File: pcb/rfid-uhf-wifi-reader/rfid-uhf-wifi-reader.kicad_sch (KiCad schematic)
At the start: 15 parts, among them P1 USB_C_Plug, Q1 BSS138, Q2 BSS138, SW1 SW_Push, SW2 SW_Push, U1 ESP32-WROOM-32, U2 AMS1117-3.3, U3 CH340E

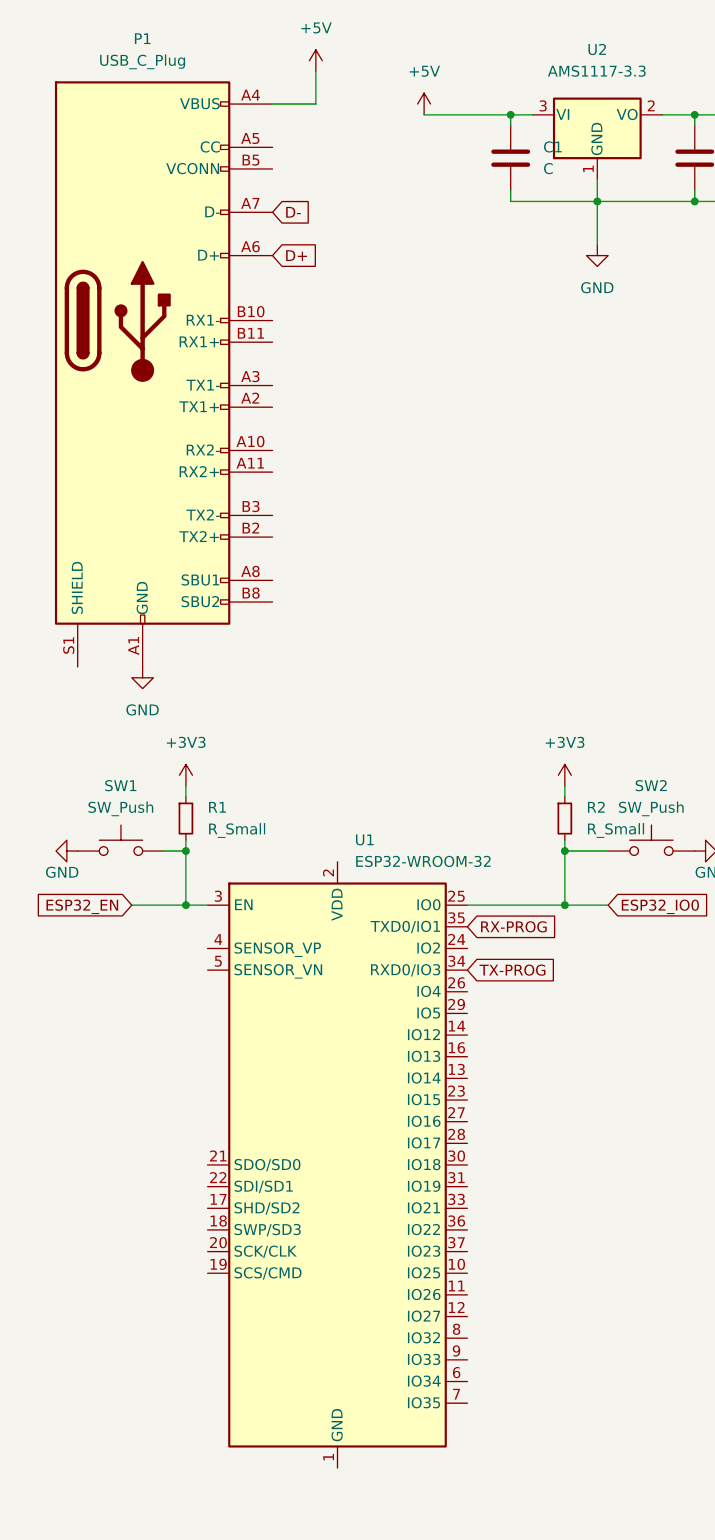
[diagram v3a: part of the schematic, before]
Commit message: update components
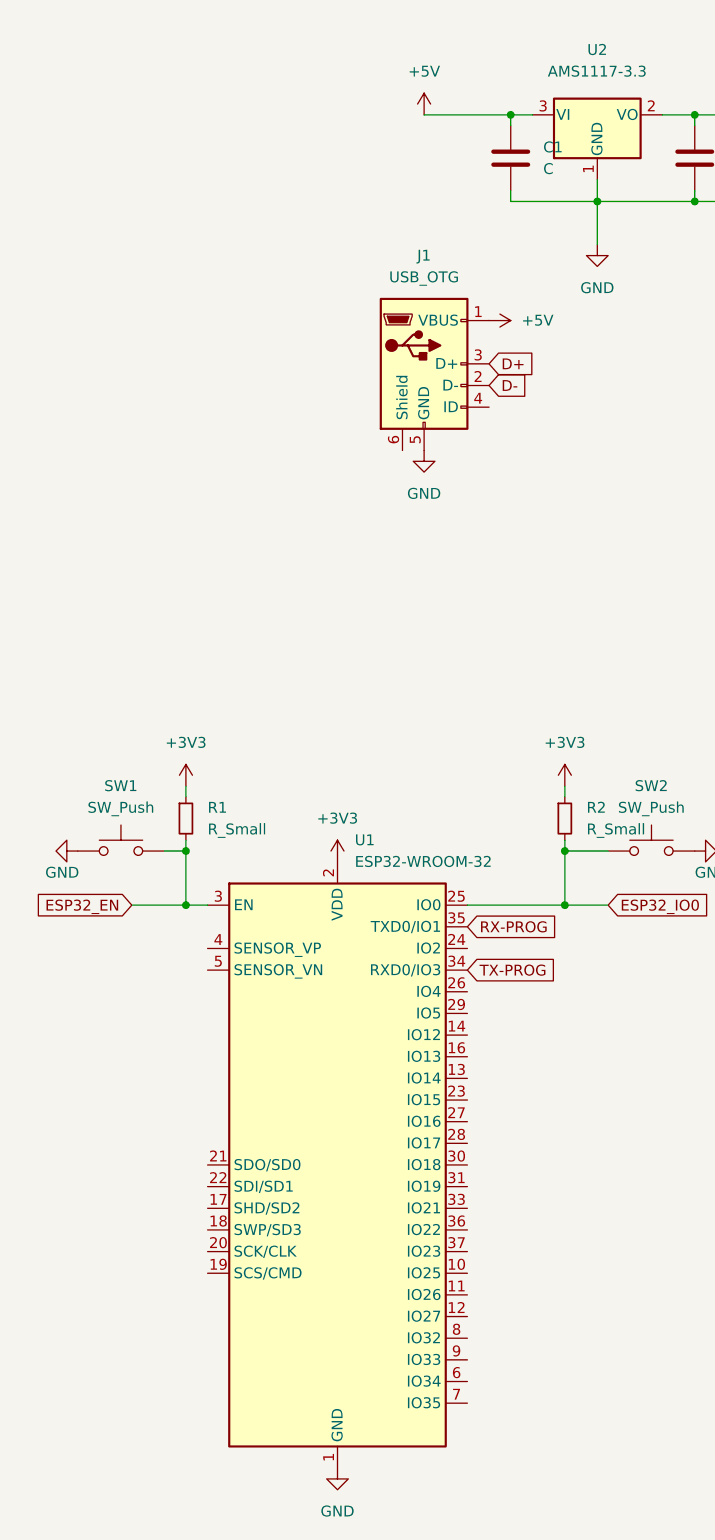
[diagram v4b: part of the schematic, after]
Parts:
- removed P1: USB_C_Plug, Connector_USB:USB_C_Plug_Molex_105444, symbol Connector:USB_C_Plug
- added J1: USB_OTG, Connector_USB:USB_Micro-B_Amphenol_10118194_Horizontal, symbol Connector:USB_OTG
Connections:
- net +3V3: now also U1.2 (VDD)
- net +5V: now also J1.1 (VBUS)
- net D+: now also J1.3 (D+)
- net D-: now also J1.2 (D-)
- net GND: now also U1.1 (GND), U1.15 (GND), U1.38 (GND), U1.39 (GND), J1.5 (GND)
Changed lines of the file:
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@@
-    (stroke (width 0) (type default) (color 0 0 0 0))
-  )
-  (wire (pts (xy 48.26 22.86) (xy 48.26 19.05))
     (stroke (width 0) (type default) (color 0 0 0 0))
   )
@@
   )
   (wire (pts (xy 101.6 33.02) (xy 101.6 34.29))
-    (stroke (width 0) (type default) (color 0 0 0 0))
-  )
-  (wire (pts (xy 43.18 22.86) (xy 48.26 22.86))
     (stroke (width 0) (type default) (color 0 0 0 0))
   )
@@
     )
   )
-  (global_label "D+" (shape input) (at 43.18 40.64 0) (fields_autoplaced)
+  (global_label "D+" (shape input) (at 68.58 53.34 0) (fields_autoplaced)
     (effects (font (size 1.27 1.27)) (justify left))
-    (property "Intersheet References" "${INTERSHEET_REFS}" (id 0) (at 48.4355 40.5606 0)
+    (property "Intersheet References" "${INTERSHEET_REFS}" (id 0) (at 73.8355 53.2606 0)
       (effects (font (size 1.27 1.27)) (justify left) hide)
     )
@@
     )
   )
-  (global_label "D-" (shape input) (at 43.18 35.56 0) (fields_autoplaced)
+  (global_label "D-" (shape input) (at 68.58 55.88 0) (fields_autoplaced)
     (effects (font (size 1.27 1.27)) (justify left))
-    (property "Intersheet References" "${INTERSHEET_REFS}" (id 0) (at 48.4355 35.4806 0)
+    (property "Intersheet References" "${INTERSHEET_REFS}" (id 0) (at 73.8355 55.8006 0)
       (effects (font (size 1.27 1.27)) (justify left) hide)
     )
@@
     )
     (property "Datasheet" "" (id 3) (at 194.31 52.07 0)
+      (effects (font (size 1.27 1.27)) hide)
+    )
+    (pin "1")
+  )
+  (symbol (lib_id "power:+3V3") (at 50.8 111.76 0) (unit 1)
+    (in_bom yes) (on_board yes) (fields_autoplaced)
+    (property "Reference" "#PWR0114" (id 0) (at 50.8 115.57 0)
+      (effects (font (size 1.27 1.27)) hide)
+    )
+    (property "Value" "+3V3" (id 1) (at 50.8 106.68 0))
+    (property "Footprint" "" (id 2) (at 50.8 111.76 0)
+      (effects (font (size 1.27 1.27)) hide)
+    )
+    (property "Datasheet" "" (id 3) (at 50.8 111.76 0)
       (effects (font (size 1.27 1.27)) hide)
     )
@@
     (pin "3")
   )
-  (symbol (lib_id "Connector:USB_C_Plug") (at 27.94 48.26 0) (unit 1)
-    (in_bom yes) (on_board yes) (fields_autoplaced)
-    (property "Reference" "P1" (id 0) (at 27.94 15.24 0))
-    (property "Value" "USB_C_Plug" (id 1) (at 27.94 17.78 0))
-    (property "Footprint" "Connector_USB:USB_C_Plug_Molex_105444" (id 2) (at 31.75 48.26 0)
-      (effects (font (size 1.27 1.27)) hide)
-    )
-    (property "Datasheet" "https://www.usb.org/sites/default/files/documents/usb_type-c.zip" (id 3) (at 31.75 48.26 0)
-      (effects (font (size 1.27 1.27)) hide)
-    )
-    (pin "A1")
-    (pin "A10")
-    (pin "A11")
-    (pin "A12")
-    (pin "A2")
-    (pin "A3")
-    (pin "A4")
-    (pin "A5")
-    (pin "A6")
-    (pin "A7")
-    (pin "A8")
-    (pin "A9")
-    (pin "B1")
-    (pin "B10")
-    (pin "B11")
-    (pin "B12")
-    (pin "B2")
-    (pin "B3")
-    (pin "B4")
-    (pin "B5")
-    (pin "B8")
-    (pin "B9")
-    (pin "S1")
+  (symbol (lib_id "power:GND") (at 50.8 182.88 0) (unit 1)
+    (in_bom yes) (on_board yes) (fields_autoplaced)
+    (property "Reference" "#PWR0115" (id 0) (at 50.8 189.23 0)
+      (effects (font (size 1.27 1.27)) hide)
+    )
+    (property "Value" "GND" (id 1) (at 50.8 187.96 0))
+    (property "Footprint" "" (id 2) (at 50.8 182.88 0)
+      (effects (font (size 1.27 1.27)) hide)
+    )
+    (property "Datasheet" "" (id 3) (at 50.8 182.88 0)
+      (effects (font (size 1.27 1.27)) hide)
+    )
+    (pin "1")
   )
   (symbol (lib_id "Device:C") (at 194.31 48.26 0) (unit 1)
@@
     (pin "9")
   )
+  (symbol (lib_id "Connector:USB_OTG") (at 60.96 53.34 0) (unit 1)
+    (in_bom yes) (on_board yes) (fields_autoplaced)
+    (property "Reference" "J1" (id 0) (at 60.96 40.64 0))
+    (property "Value" "USB_OTG" (id 1) (at 60.96 43.18 0))
+    (property "Footprint" "Connector_USB:USB_Micro-B_Amphenol_10118194_Horizontal" (id 2) (at 64.77 54.61 0)
+      (effects (font (size 1.27 1.27)) hide)
+    )
+    (property "Datasheet" " ~" (id 3) (at 64.77 54.61 0)
+      (effects (font (size 1.27 1.27)) hide)
+    )
+    (pin "1")
+    (pin "2")
+    (pin "3")
+    (pin "4")
+    (pin "5")
+    (pin "6")
+  )
   (symbol (lib_id "power:+3V3") (at 77.47 102.87 0) (unit 1)
     (in_bom yes) (on_board yes) (fields_autoplaced)
@@
     (pin "2")
   )
-  (symbol (lib_id "power:GND") (at 27.94 88.9 0) (unit 1)
-    (in_bom yes) (on_board yes) (fields_autoplaced)
-    (property "Reference" "#PWR0109" (id 0) (at 27.94 95.25 0)
-      (effects (font (size 1.27 1.27)) hide)
-    )
-    (property "Value" "GND" (id 1) (at 27.94 93.98 0))
-    (property "Footprint" "" (id 2) (at 27.94 88.9 0)
-      (effects (font (size 1.27 1.27)) hide)
-    )
-    (property "Datasheet" "" (id 3) (at 27.94 88.9 0)
+  (symbol (lib_id "power:GND") (at 60.96 63.5 0) (unit 1)
+    (in_bom yes) (on_board yes) (fields_autoplaced)
+    (property "Reference" "#PWR0109" (id 0) (at 60.96 69.85 0)
+      (effects (font (size 1.27 1.27)) hide)
+    )
+    (property "Value" "GND" (id 1) (at 60.96 68.58 0))
+    (property "Footprint" "" (id 2) (at 60.96 63.5 0)
+      (effects (font (size 1.27 1.27)) hide)
+    )
+    (property "Datasheet" "" (id 3) (at 60.96 63.5 0)
       (effects (font (size 1.27 1.27)) hide)
     )
@@
     (pin "1")
   )
-  (symbol (lib_id "power:+5V") (at 48.26 19.05 0) (unit 1)
-    (in_bom yes) (on_board yes) (fields_autoplaced)
-    (property "Reference" "#PWR0108" (id 0) (at 48.26 22.86 0)
-      (effects (font (size 1.27 1.27)) hide)
-    )
-    (property "Value" "+5V" (id 1) (at 48.26 13.97 0))
-    (property "Footprint" "" (id 2) (at 48.26 19.05 0)
-      (effects (font (size 1.27 1.27)) hide)
-    )
-    (property "Datasheet" "" (id 3) (at 48.26 19.05 0)
+  (symbol (lib_id "power:+5V") (at 68.58 48.26 270) (unit 1)
+    (in_bom yes) (on_board yes) (fields_autoplaced)
+    (property "Reference" "#PWR0108" (id 0) (at 64.77 48.26 0)
+      (effects (font (size 1.27 1.27)) hide)
+    )
+    (property "Value" "+5V" (id 1) (at 72.39 48.2599 90)
+      (effects (font (size 1.27 1.27)) (justify left))
+    )
+    (property "Footprint" "" (id 2) (at 68.58 48.26 0)
+      (effects (font (size 1.27 1.27)) hide)
+    )
+    (property "Datasheet" "" (id 3) (at 68.58 48.26 0)
       (effects (font (size 1.27 1.27)) hide)
     )
@@
       (reference "#PWR0113") (unit 1) (value "GND") (footprint "")
     )
+    (path "/11ba5ea4-6fdf-445f-95f3-89c5075ff57c"
+      (reference "#PWR0114") (unit 1) (value "+3V3") (footprint "")
+    )
+    (path "/c6821f6d-ae1c-499e-ad7d-74e9a034a4b5"
+      (reference "#PWR0115") (unit 1) (value "GND") (footprint "")
+    )
     (path "/74f5e97e-4553-4de3-a8be-4168a7d4a4b0"
       (reference "C1") (unit 1) (value "C") (footprint "Capacitor_SMD:C_0603_1608Metric")
@@
       (reference "C5") (unit 1) (value "C") (footprint "Capacitor_SMD:C_0603_1608Metric")
     )
-    (path "/c7fcd3ed-2f64-4cc5-b178-58d652bdbddb"
-      (reference "P1") (unit 1) (value "USB_C_Plug") (footprint "Connector_USB:USB_C_Plug_Molex_105444")
+    (path "/da4349c5-9342-4c74-8c10-cca4c3af9ad1"
+      (reference "J1") (unit 1) (value "USB_OTG") (footprint "Connector_USB:USB_Micro-B_Amphenol_10118194_Horizontal")
     )
     (path "/b5bc826a-1504-4d26-a138-ddec82e63711"

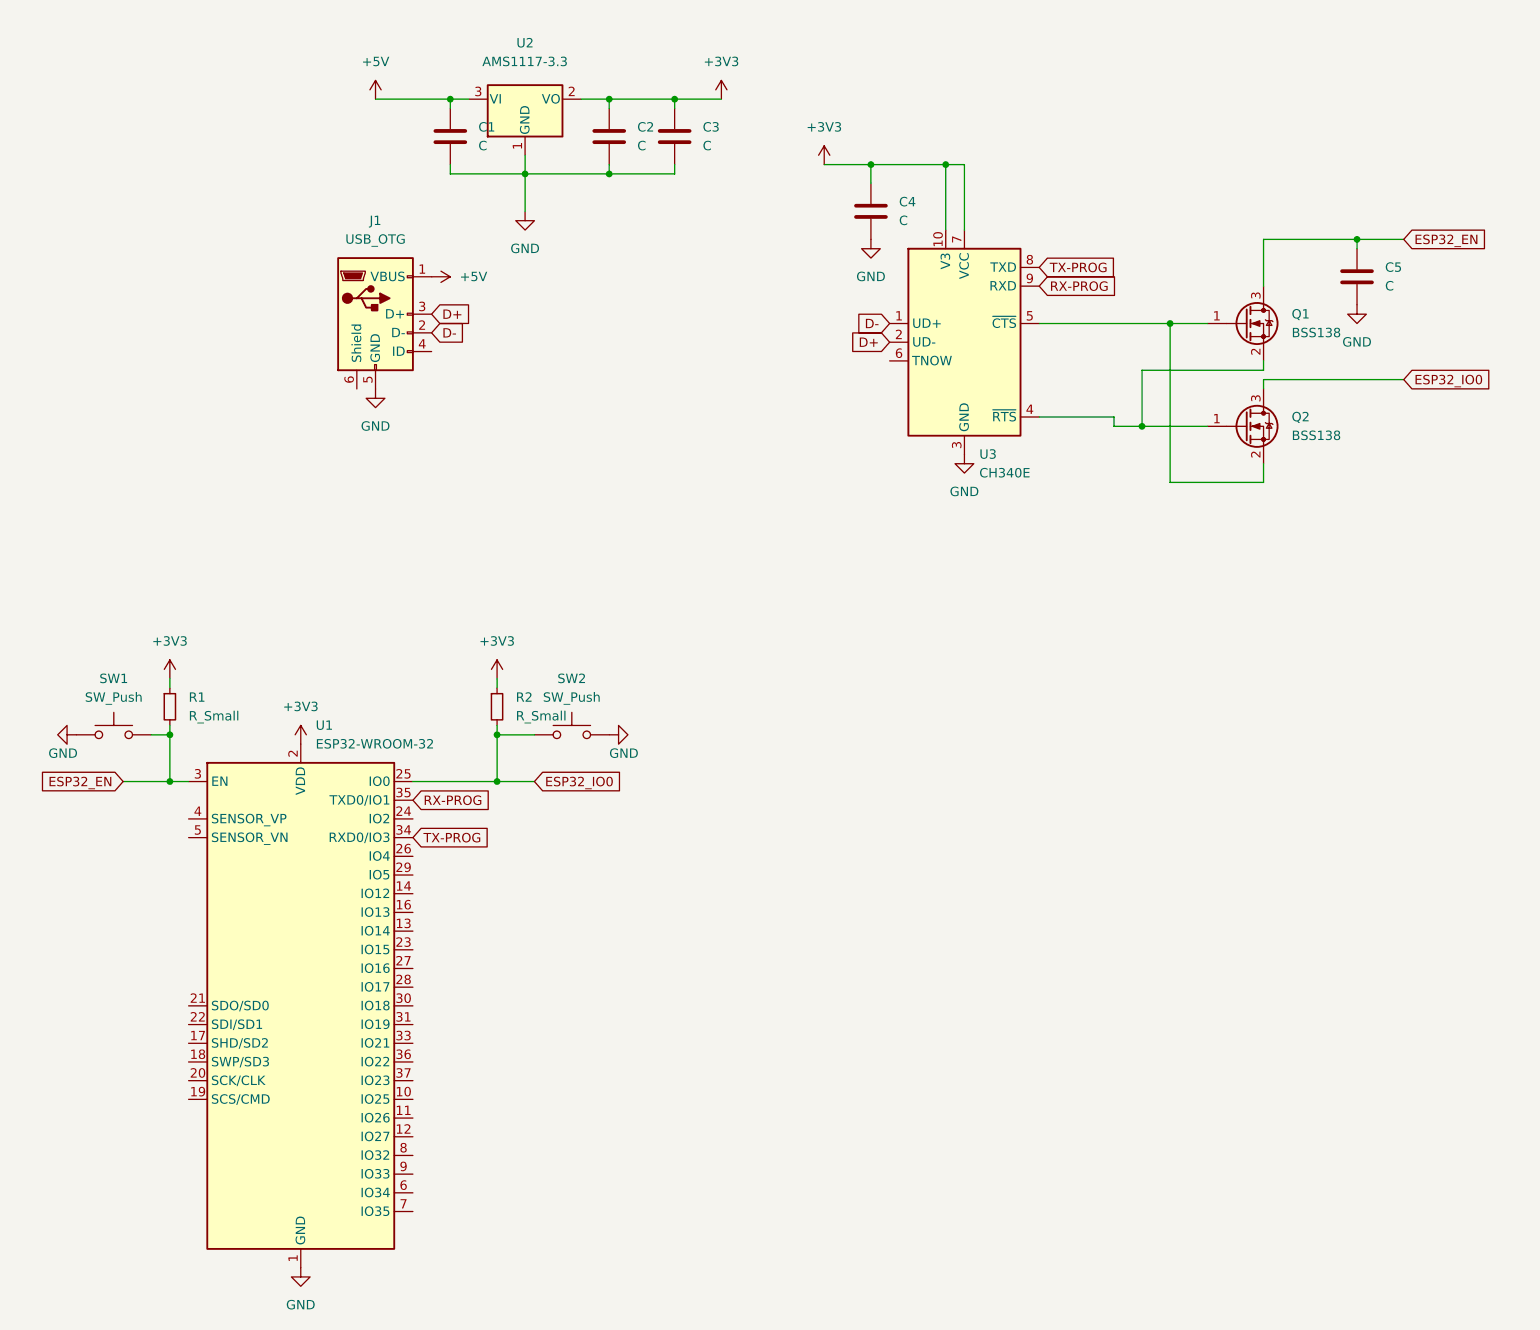
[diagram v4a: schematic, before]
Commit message: add leds
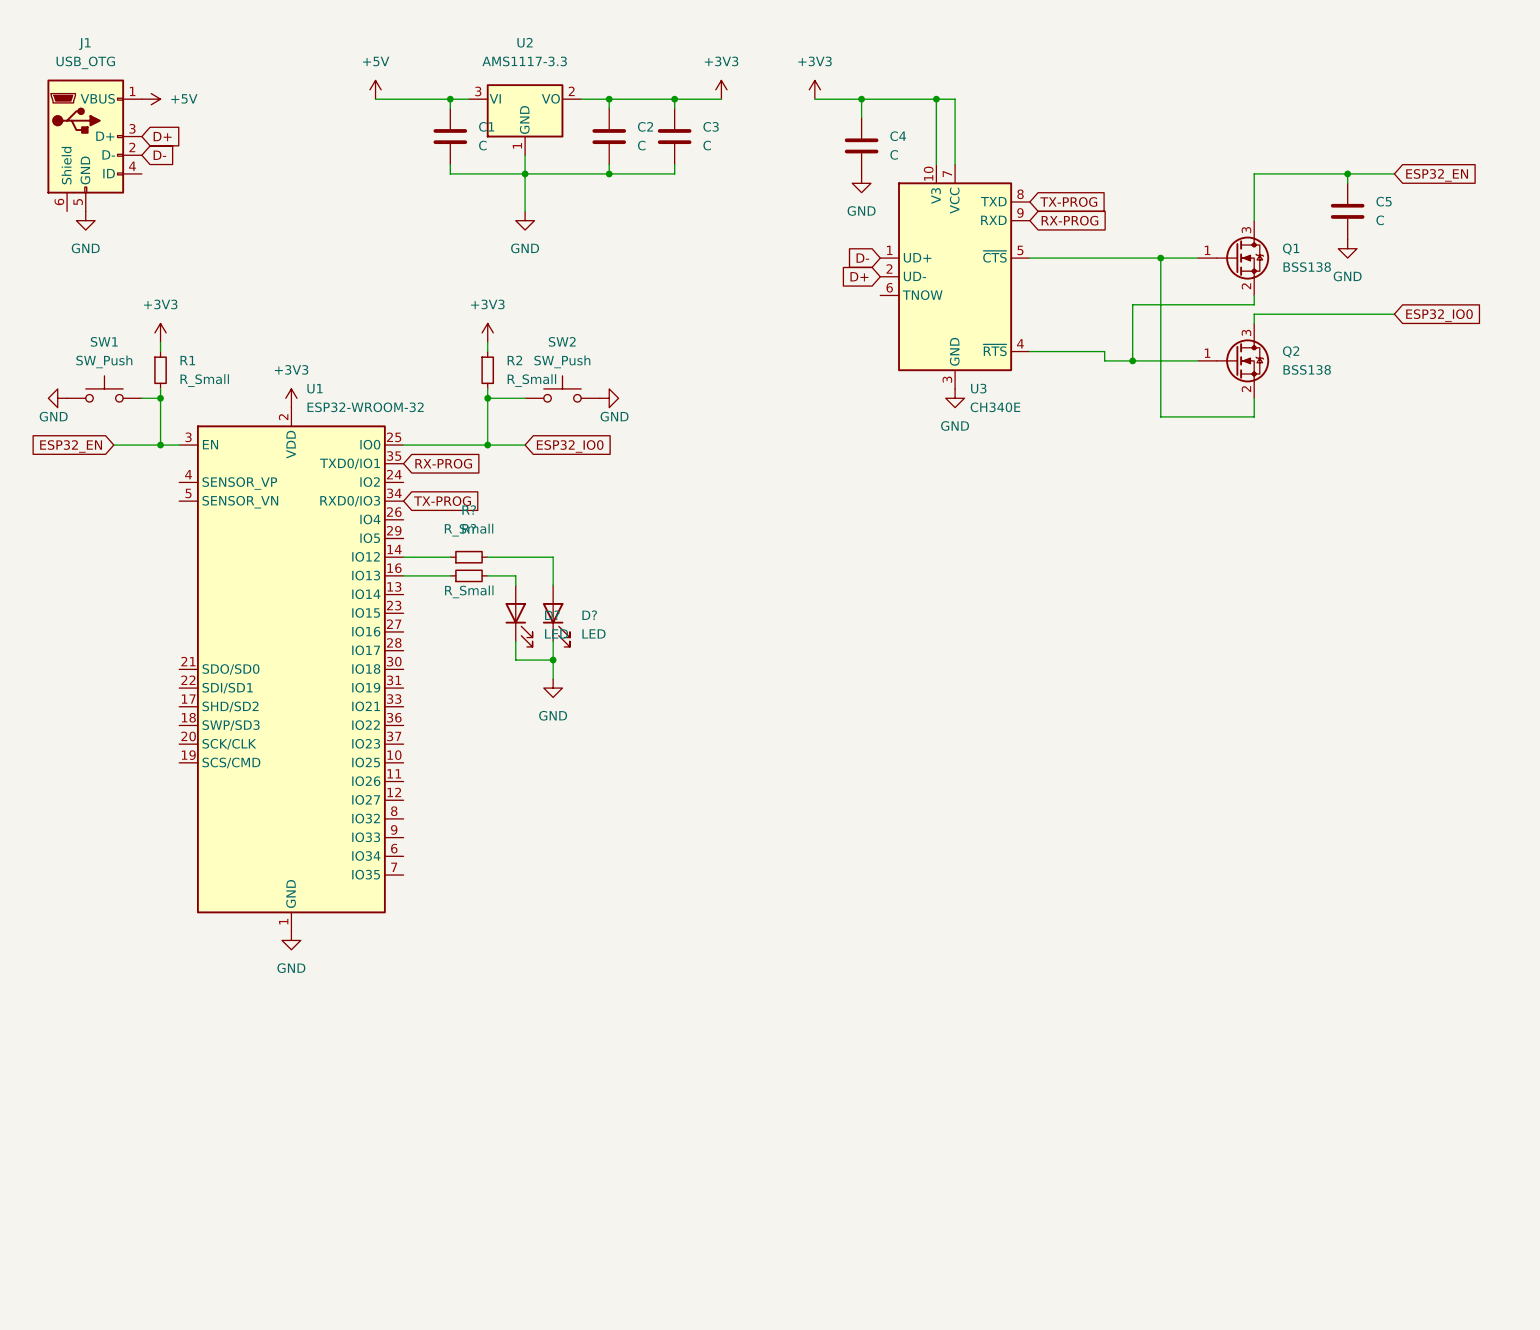
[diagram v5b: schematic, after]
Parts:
- added D? (x2): LED, symbol Device:LED
- added R? (x2): R_Small, Resistor_SMD:R_0603_1608Metric, symbol Device:R_Small
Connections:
- net GND: now also D?.1 (K), D?.1 (K)
- net at U1.14 (IO12): now also R?.1
- net at U1.16 (IO13): now also R?.1
- new net: D?.2 (A), R?.2 (x2)
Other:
- moved on the sheet: C4, C5, J1, Q1, Q2, R1, R2, SW1, SW2, U1, U3
